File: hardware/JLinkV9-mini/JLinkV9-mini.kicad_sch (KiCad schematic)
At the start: 60 parts, among them J1 USB_C_Receptacle_USB2.0, J2 Conn_01x04, J3 Conn_01x04, J4 Conn_01x07, Q1 NEC3400, U1 ME6210A33M3G, U2 STM32F207VET6, Y1 12M

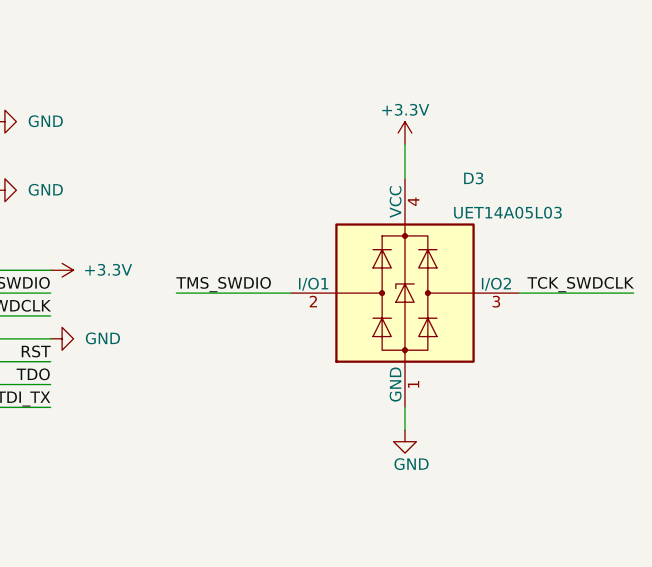
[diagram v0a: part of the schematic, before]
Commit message: feat: update jlinkv9-mini pcb
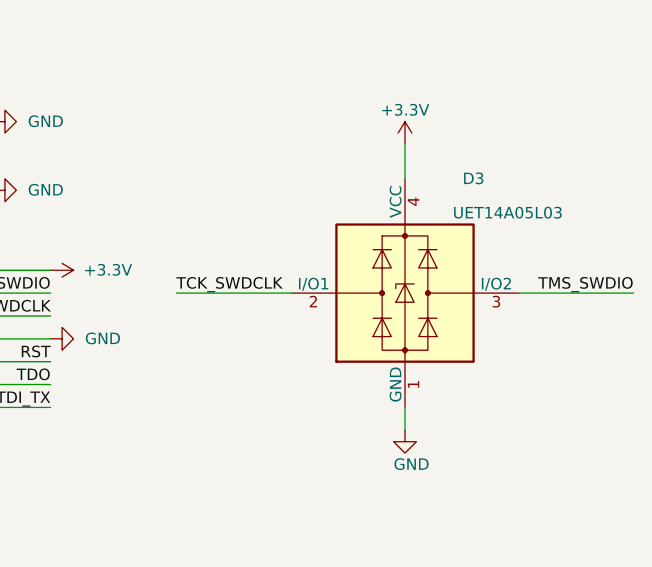
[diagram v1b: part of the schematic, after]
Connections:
- net TCK_SWDCLK: now also D3.2 (I/O1); no longer D3.3 (I/O2)
- net TMS_SWDIO: now also D3.3 (I/O2); no longer D3.2 (I/O1)
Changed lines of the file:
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@@
+    (effects (font (size 1.27 1.27)) (justify left bottom))
+  )
+  (label "TCK_SWDCLK" (at 231.14 137.16 0)
     (effects (font (size 1.27 1.27)) (justify left bottom))
   )
@@
   (label "TDI_TX" (at 210.82 120.65 180)
     (effects (font (size 1.27 1.27)) (justify right bottom))
-  )
-  (label "TMS_SWDIO" (at 231.14 137.16 0)
-    (effects (font (size 1.27 1.27)) (justify left bottom))
   )
   (label "SWDIO" (at 72.39 175.26 180)
@@
     (effects (font (size 1.27 1.27)) (justify left bottom))
   )
+  (label "TMS_SWDIO" (at 281.94 137.16 180)
+    (effects (font (size 1.27 1.27)) (justify right bottom))
+  )
   (label "PA7" (at 97.79 36.83 0)
     (effects (font (size 1.27 1.27)) (justify left bottom))
@@
     (effects (font (size 1.27 1.27)) (justify left bottom))
   )
-  (label "TCK_SWDCLK" (at 281.94 137.16 180)
-    (effects (font (size 1.27 1.27)) (justify right bottom))
-  )
   (label "TDO" (at 217.17 147.32 180)
